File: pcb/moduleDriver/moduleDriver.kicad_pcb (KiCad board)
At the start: 2 copper layers, 70 x 80 mm, 43 parts, among them J1 MOTOR, J10 Sensor, J11 Power, J12 Power, J13 Power, J2 MOTOR, J3 MOTOR, J4 MOTOR, J5 IDC, J6 IDC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

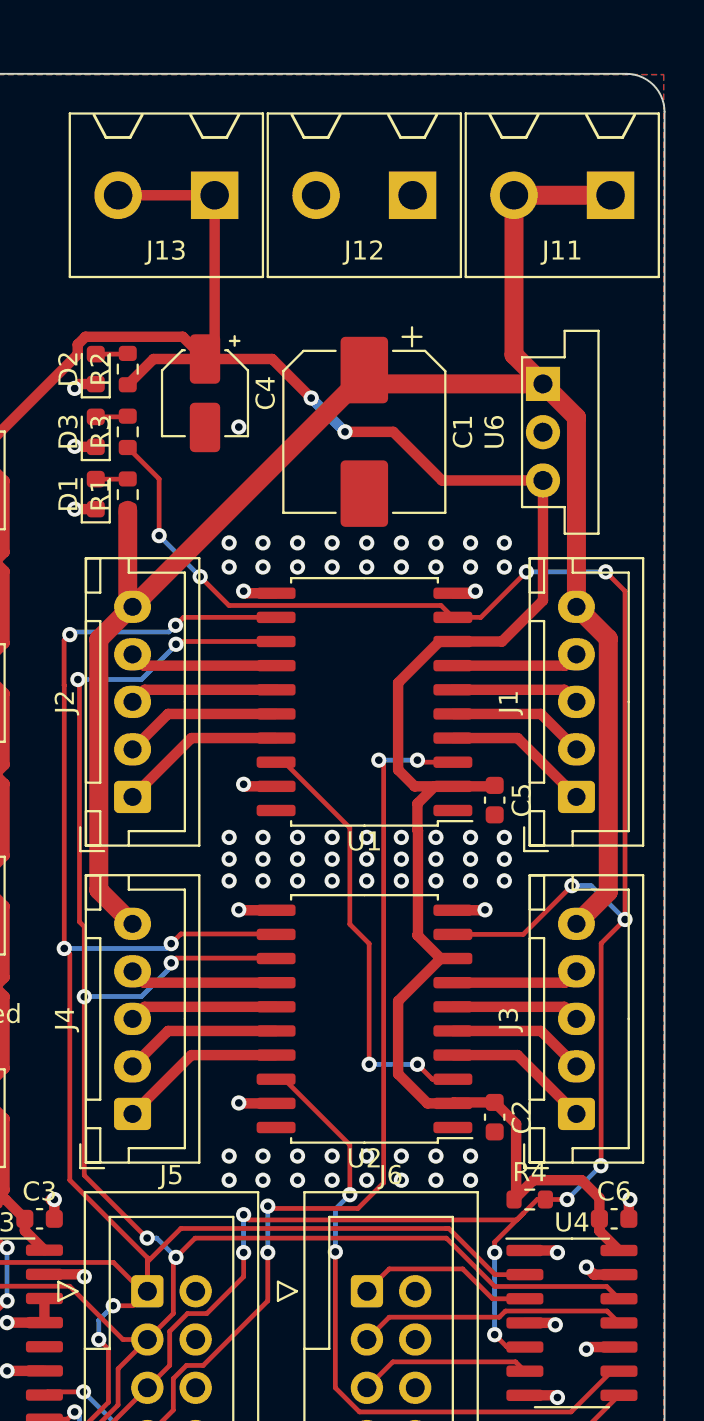
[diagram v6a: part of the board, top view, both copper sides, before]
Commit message: Fix gap between power connectors
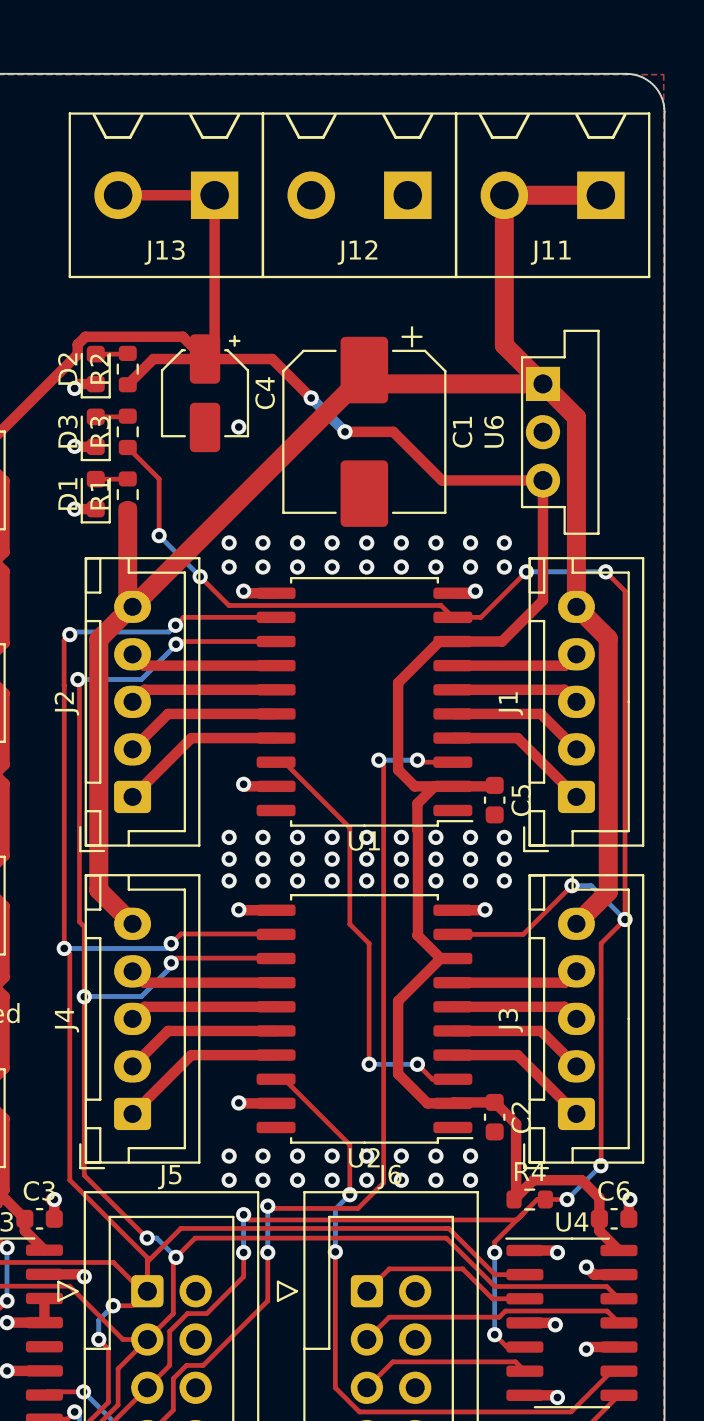
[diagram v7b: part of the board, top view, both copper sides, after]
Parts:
- moved J11 0.51 mm to (136.7, 56.4)
- moved J12 0.25 mm to (126.5, 56.4)
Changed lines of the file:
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@@
       (layerselection 0x00010fc_ffffffff)
       (disableapertmacros false)
-      (usegerberextensions false)
-      (usegerberattributes true)
-      (usegerberadvancedattributes true)
-      (creategerberjobfile true)
+      (usegerberextensions true)
+      (usegerberattributes false)
+      (usegerberadvancedattributes false)
+      (creategerberjobfile false)
       (svguseinch false)
       (svgprecision 6)
@@
       (psa4output false)
       (plotreference true)
-      (plotvalue true)
+      (plotvalue false)
       (plotinvisibletext false)
       (sketchpadsonfab false)
-      (subtractmaskfromsilk false)
+      (subtractmaskfromsilk true)
       (outputformat 1)
       (mirror false)
-      (drillshape 1)
+      (drillshape 0)
       (scaleselection 1)
-      (outputdirectory "")
+      (outputdirectory "jlcpcb/")
     )
   )
@@
     (fp_line (start 12.45 -2.35) (end -2.45 -2.35) (layer "F.Fab") (width 0.1))
     (fp_line (start -0.625 -2.35) (end 0 -1.35) (layer "F.Fab") (width 0.1))
-    (pad "1" thru_hole roundrect locked (at 0 0 90) (size 1.7 1.95) (drill 0.95) (layers *.Cu *.Mask) (roundrect_rratio 0.147059)
+    (pad "1" thru_hole roundrect locked (at 0 0 90) (size 1.7 1.95) (drill 0.95) (layers *.Cu *.Mask) (roundrect_rratio 0.1470588235)
       (net 14 "/MOTOR_C_PHASE_A") (pinfunction "Pin_1") (pintype "passive"))
     (pad "2" thru_hole oval locked (at 2.5 0 90) (size 1.7 1.95) (drill 0.95) (layers *.Cu *.Mask)
@@
     (fp_line (start 4.52 14.07) (end -1.98 14.07) (layer "F.Fab") (width 0.1))
     (fp_line (start 4.52 -3.91) (end 4.52 14.07) (layer "F.Fab") (width 0.1))
-    (pad "1" thru_hole roundrect locked (at 0 0) (size 1.7 1.7) (drill 1) (layers *.Cu *.Mask) (roundrect_rratio 0.147059)
+    (pad "1" thru_hole roundrect locked (at 0 0) (size 1.7 1.7) (drill 1) (layers *.Cu *.Mask) (roundrect_rratio 0.1470588235)
       (net 25 "/LATCH_IN") (pinfunction "Pin_1") (pintype "passive"))
     (pad "2" thru_hole circle locked (at 2.54 0) (size 1.7 1.7) (drill 1) (layers *.Cu *.Mask)
@@
     (fp_line (start 12.45 3.4) (end 12.45 -2.35) (layer "F.Fab") (width 0.1))
     (fp_line (start -2.45 -2.35) (end -2.45 3.4) (layer "F.Fab") (width 0.1))
-    (pad "1" thru_hole roundrect locked (at 0 0 90) (size 1.7 1.95) (drill 0.95) (layers *.Cu *.Mask) (roundrect_rratio 0.147059)
+    (pad "1" thru_hole roundrect locked (at 0 0 90) (size 1.7 1.95) (drill 0.95) (layers *.Cu *.Mask) (roundrect_rratio 0.1470588235)
       (net 6 "/MOTOR_A_PHASE_A") (pinfunction "Pin_1") (pintype "passive"))
     (pad "2" thru_hole oval locked (at 2.5 0 90) (size 1.7 1.95) (drill 0.95) (layers *.Cu *.Mask)
@@
   )
   (footprint "Library:ScrewTerminal-5.08-2P" locked (layer "F.Cu")
-    (at 126.746 56.388 180)
+    (at 126.492 56.388 180)
     (property "Sheetfile" "moduleDriver.kicad_sch")
     (property "Sheetname" "")
@@
     (fp_line (start 12.45 3.4) (end 12.45 -2.35) (layer "F.Fab") (width 0.1))
     (fp_line (start -0.625 -2.35) (end 0 -1.35) (layer "F.Fab") (width 0.1))
-    (pad "1" thru_hole roundrect locked (at 0 0 90) (size 1.7 1.95) (drill 0.95) (layers *.Cu *.Mask) (roundrect_rratio 0.147059)
+    (pad "1" thru_hole roundrect locked (at 0 0 90) (size 1.7 1.95) (drill 0.95) (layers *.Cu *.Mask) (roundrect_rratio 0.1470588235)
       (net 10 "/MOTOR_B_PHASE_A") (pinfunction "Pin_1") (pintype "passive"))
     (pad "2" thru_hole oval locked (at 2.5 0 90) (size 1.7 1.95) (drill 0.95) (layers *.Cu *.Mask)
@@
   )
   (footprint "Library:ScrewTerminal-5.08-2P" locked (layer "F.Cu")
-    (at 137.16 56.388 180)
+    (at 136.652 56.388 180)
     (property "Sheetfile" "moduleDriver.kicad_sch")
     (property "Sheetname" "")
@@
     (fp_line (start -2.45 -2.35) (end -2.45 3.4) (layer "F.Fab") (width 0.1))
     (fp_line (start -0.625 -2.35) (end 0 -1.35) (layer "F.Fab") (width 0.1))
-    (pad "1" thru_hole roundrect locked (at 0 0 90) (size 1.7 1.95) (drill 0.95) (layers *.Cu *.Mask) (roundrect_rratio 0.147059)
+    (pad "1" thru_hole roundrect locked (at 0 0 90) (size 1.7 1.95) (drill 0.95) (layers *.Cu *.Mask) (roundrect_rratio 0.1470588235)
       (net 18 "/MOTOR_D_PHASE_A") (pinfunction "Pin_1") (pintype "passive"))
     (pad "2" thru_hole oval locked (at 2.5 0 90) (size 1.7 1.95) (drill 0.95) (layers *.Cu *.Mask)
@@
     (fp_line (start -3.18 15.26) (end -3.18 -4.1) (layer "F.Fab") (width 0.1))
     (fp_line (start -1.98 3.03) (end -1.98 -3.91) (layer "F.Fab") (width 0.1))
-    (pad "1" thru_hole roundrect locked (at 0 0) (size 1.7 1.7) (drill 1) (layers *.Cu *.Mask) (roundrect_rratio 0.147059)
+    (pad "1" thru_hole roundrect locked (at 0 0) (size 1.7 1.7) (drill 1) (layers *.Cu *.Mask) (roundrect_rratio 0.1470588235)
       (net 30 "/LATCH_OUT") (pinfunction "Pin_1") (pintype "passive"))
     (pad "2" thru_hole circle locked (at 2.54 0) (size 1.7 1.7) (drill 1) (layers *.Cu *.Mask)
@@
   (gr_line (start 100 69) (end 100 52) (layer "Edge.Cuts") (width 0.1))
   (segment (start 111.76 77.7855) (end 112.014 78.0395) (width 1) (layer "F.Cu") (net 1))
+  (segment (start 131.572 64.27825) (end 133.605 66.31125) (width 1) (layer "F.Cu") (net 1))
   (segment (start 137.04 93.04275) (end 135.365 94.71775) (width 1) (layer "F.Cu") (net 1))
   (segment (start 111.9525 78.0395) (end 112.014 78.0395) (width 1) (layer "F.Cu") (net 1))
+  (segment (start 131.572 56.388) (end 136.652 56.388) (width 1) (layer "F.Cu") (net 1))
   (segment (start 124.206 65.8475) (end 112.014 78.0395) (width 1) (layer "F.Cu") (net 1))
   (segment (start 137.04 79.7145) (end 137.04 93.04275) (width 1) (layer "F.Cu") (net 1))
-  (segment (start 137.16 56.388) (end 132.08 56.388) (width 1) (layer "F.Cu") (net 1))
   (segment (start 135.365 78.0395) (end 137.04 79.7145) (width 1) (layer "F.Cu") (net 1))
+  (segment (start 131.572 56.388) (end 131.572 64.27825) (width 1) (layer "F.Cu") (net 1))
   (segment (start 110.236 79.756) (end 111.9525 78.0395) (width 1) (layer "F.Cu") (net 1))
   (segment (start 133.605 66.31125) (end 135.365 68.07125) (width 1) (layer "F.Cu") (net 1))
-  (segment (start 132.08 56.388) (end 132.08 64.78625) (width 1) (layer "F.Cu") (net 1))
   (segment (start 133.605 66.31125) (end 124.93325 66.31125) (width 1) (layer "F.Cu") (net 1))
   (segment (start 124.206 65.584) (end 124.206 65.8475) (width 1) (layer "F.Cu") (net 1))
   (segment (start 110.236 92.93975) (end 110.236 79.756) (width 1) (layer "F.Cu") (net 1))
   (segment (start 111.76 72.961) (end 111.76 77.7855) (width 1) (layer "F.Cu") (net 1))
-  (segment (start 132.08 64.78625) (end 133.605 66.31125) (width 1) (layer "F.Cu") (net 1))
   (segment (start 135.365 68.07125) (end 135.365 78.0395) (width 1) (layer "F.Cu") (net 1))
   (segment (start 112.014 94.71775) (end 110.236 92.93975) (width 1) (layer "F.Cu") (net 1))

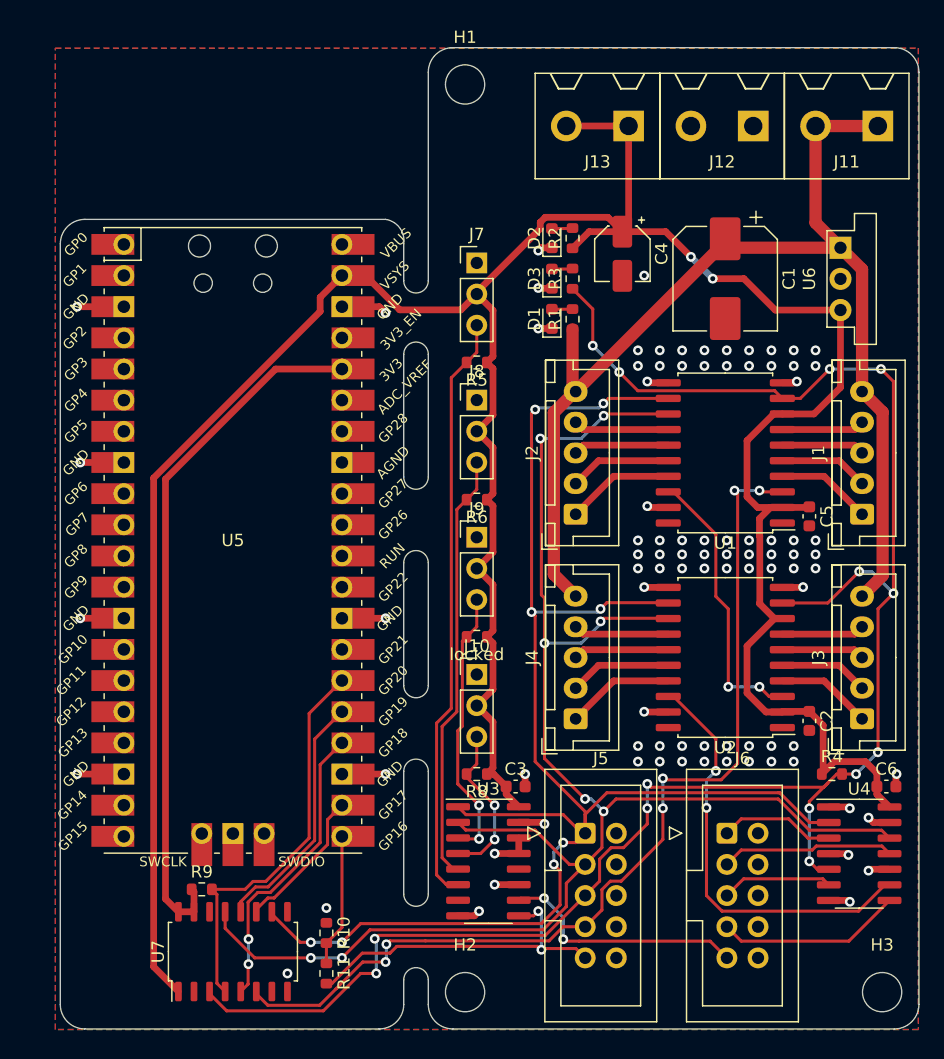
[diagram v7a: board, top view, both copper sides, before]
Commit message: Top silkscreen
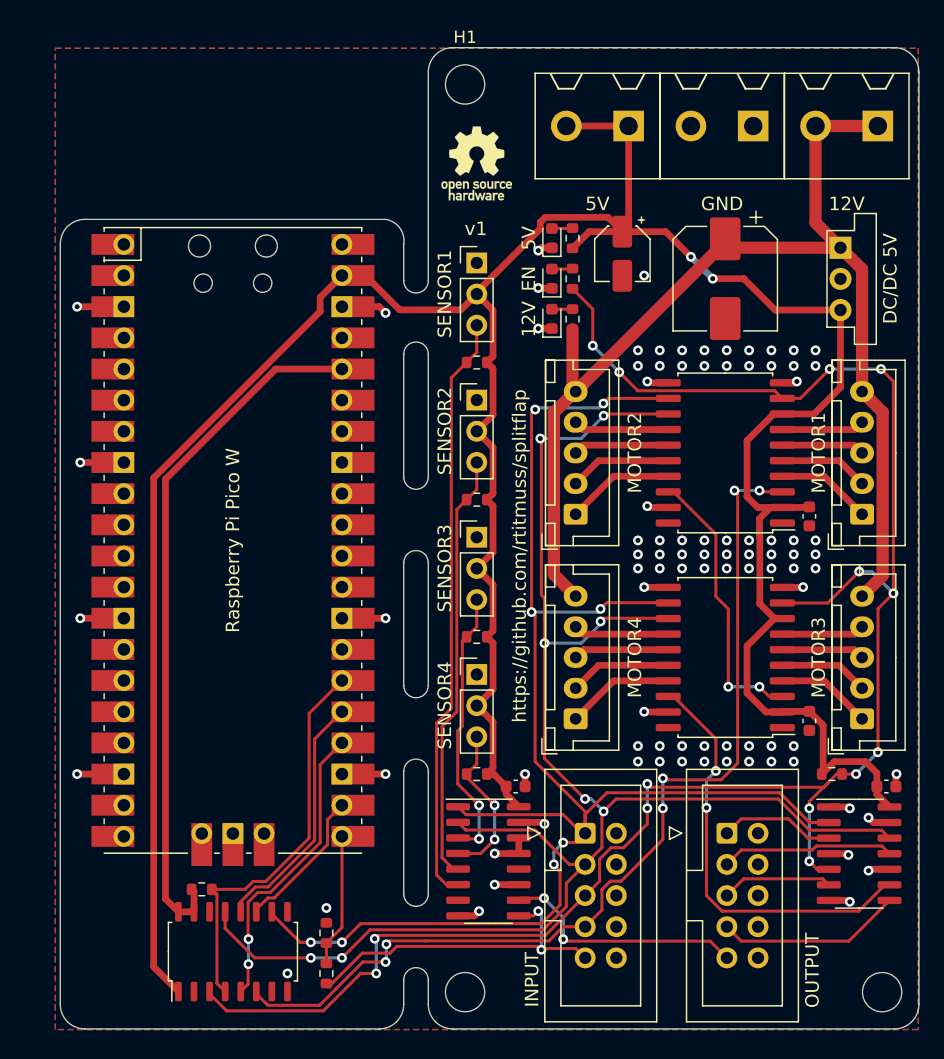
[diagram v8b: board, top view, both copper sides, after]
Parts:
- added REF**: OSHW-Logo_5.7x6mm_SilkScreen, Symbol:OSHW-Logo_5.7x6mm_SilkScreen, F.Cu at (103.9, 59.4)
- R1: value 220R -> 200R
- R10: value 2k -> 2.4k
- R11: value 1k -> 1.2k
- R2, R3: value 220R -> 510R
- R9: value 5k -> 5.1k
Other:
- board text added: "12V"
- board text added: "5V"
- board text added: "DC/DC 5V"
- board text added: "EN"
- board text added: "GND"
- board text added: "INPUT"
- board text added: "MOTOR1"
- board text added: "MOTOR2"
- board text added: "MOTOR3"
- board text added: "MOTOR4"
- board text added: "OUTPUT"
- board text added: "Raspberry Pi Pico W"
- board text added: "SENSOR1"
- board text added: "SENSOR2"
- board text added: "SENSOR3"
- board text added: "SENSOR4"
- board text added: "https://github.com/rtitmuss/splitflap"
- board text added: "v1"
